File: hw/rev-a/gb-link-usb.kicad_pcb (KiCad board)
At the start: 2 copper layers, 52 x 51 mm, 43 parts, among them J1 10103594-0001LF, J2 TSW-118-07-L-D, J3 TSW-118-07-L-D, J4 SM03B-SRSS-TB(LF)(SN), SW1 434133025816, SW2 434133025816, U1 RP2350A, U2 NCP1117ST33T3G, U3 W25Q128JVSIQ, X1 12MHz

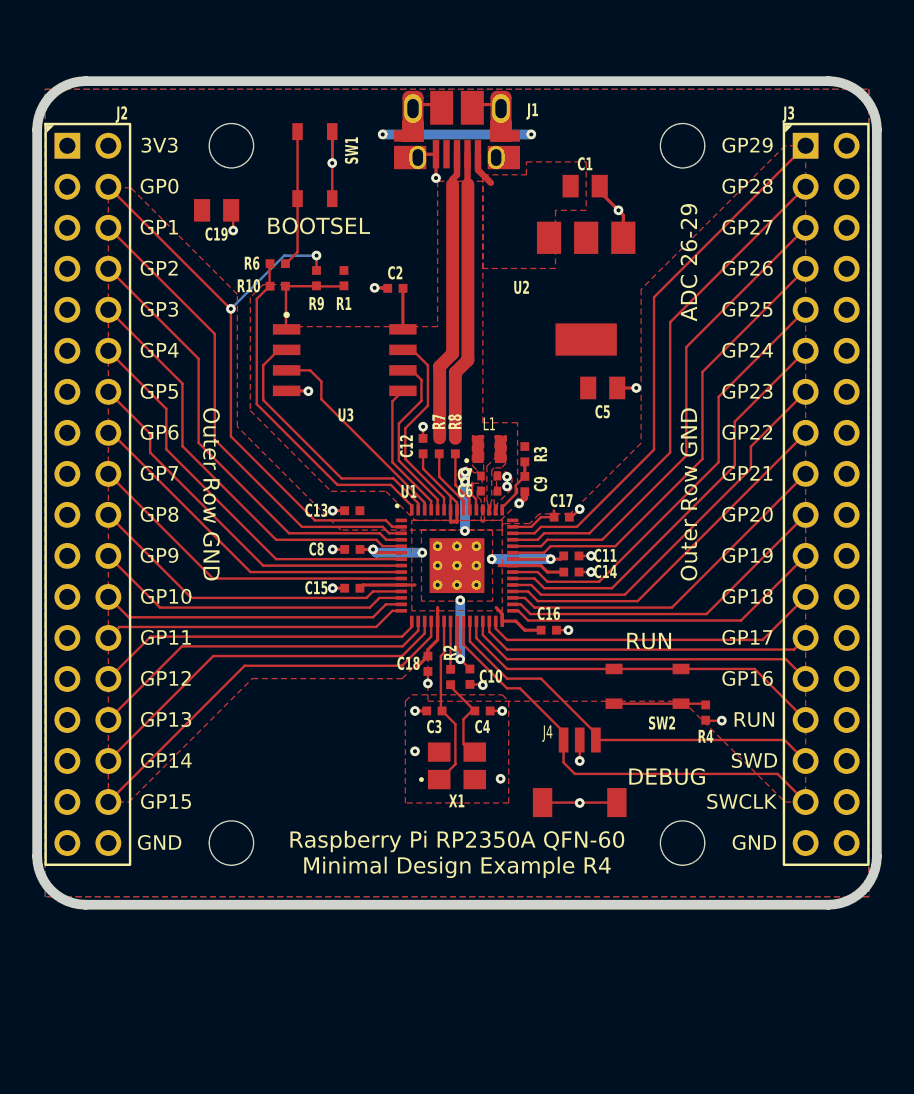
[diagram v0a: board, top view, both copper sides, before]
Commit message: PCB rev A routed: scripted build + Freerouting pipeline, DRC 0 errors
Co-Authored-By: Claude Opus 5.5 (1M context) <noreply@anthropic.com>
Claude-Session: https://claude.ai/code/session_01MZ3uQJCcn6FcjzVDhZnLJN
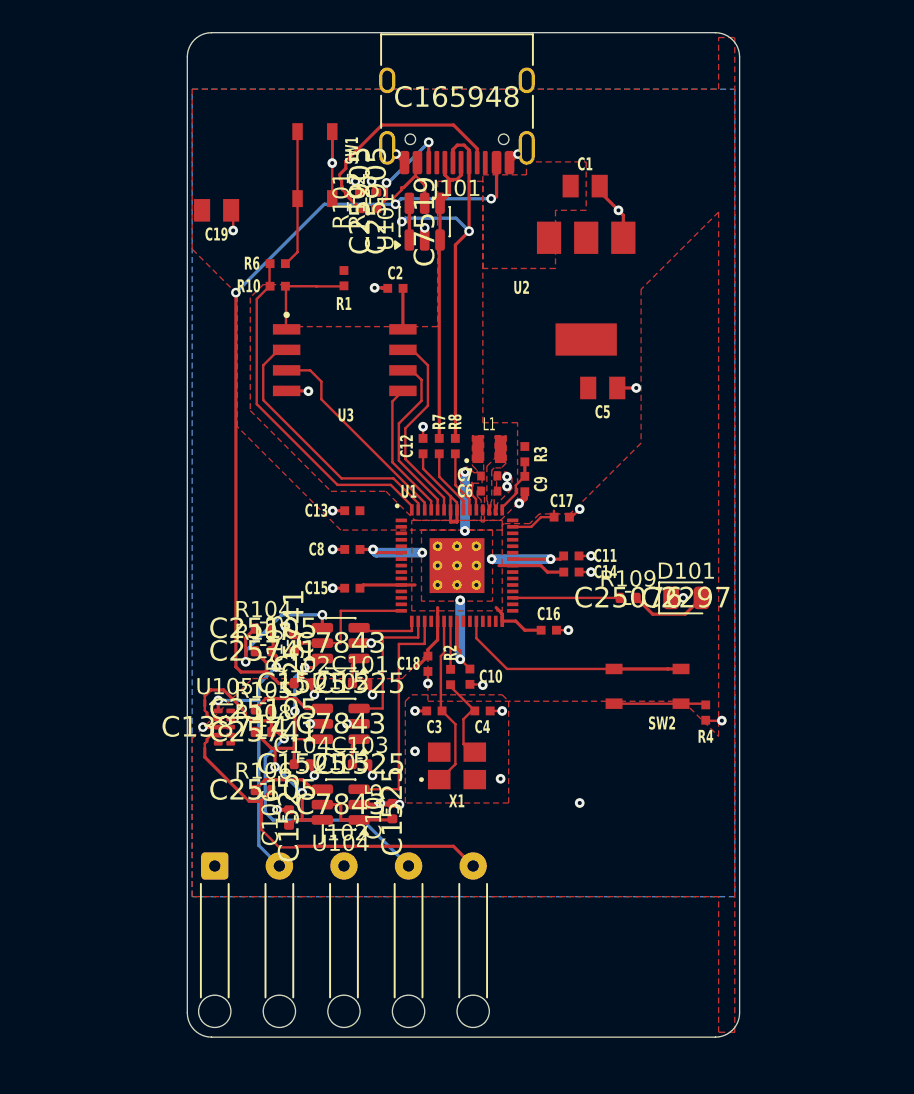
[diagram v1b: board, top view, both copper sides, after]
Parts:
- removed J1: 10103594-0001LF, RPI_COMPILED:amphenol_10103594-0001lf
- removed J2, J3: TSW-118-07-L-D, RPI_COMPILED:samtec_tsw-118-07-l-d
- removed J4: SM03B-SRSS-TB(LF)(SN), RPI_COMPILED:jst_sm03b-srss-tb-lf--sn-
- removed MH1, MH2, MH3, MH4: NPTH FD2.75mm SM3.15mm KO6mm, RPI_COMPILED:none_mh_npth_fd2p75mm_sm3p15mm_ko6mm
- removed R9: 0, RPI_COMPILED:generic_resc1005x35
- added C101: 100n, Capacitor_SMD:C_0402_1005Metric, F.Cu at (94.0, 107.3)
- added C102: 100n, Capacitor_SMD:C_0402_1005Metric, F.Cu at (90.4, 107.3)
- added C103: 100n, Capacitor_SMD:C_0402_1005Metric, F.Cu at (94.0, 112.3)
- added C104: 100n, Capacitor_SMD:C_0402_1005Metric, F.Cu at (90.4, 112.3)
- added C105: 100n, Capacitor_SMD:C_0402_1005Metric, F.Cu at (96.0, 115.2)
- added C106: 100n, Capacitor_SMD:C_0402_1005Metric, F.Cu at (89.6, 115.6)
- added D101: green, LED_SMD:LED_0805_2012Metric, F.Cu at (114.2, 102.0)
- added J101: TYPE-C-31-M-12, Connector_USB:USB_C_Receptacle_HRO_TYPE-C-31-M-12, F.Cu at (100.0, 71.0)
- added J102: Link cable, Connector_Wire:SolderWire-0.15sqmm_1x05_P4mm_D0.5mm_OD1.5mm_Relief, F.Cu at (85.0, 118.6)
- added R101: 5.1k, Resistor_SMD:R_0402_1005Metric, F.Cu at (94.0, 77.4)
- added R102: 5.1k, Resistor_SMD:R_0402_1005Metric, F.Cu at (95.0, 77.4)
- added R103: 100k, Resistor_SMD:R_0402_1005Metric, F.Cu at (89.9, 104.8)
- added R104: 33, Resistor_SMD:R_0402_1005Metric, F.Cu at (88.0, 103.9)
- added R105: 33, Resistor_SMD:R_0402_1005Metric, F.Cu at (88.0, 108.9)
- added R106: 33, Resistor_SMD:R_0402_1005Metric, F.Cu at (88.0, 113.9)
- added R107: 100k, Resistor_SMD:R_0402_1005Metric, F.Cu at (88.0, 105.3)
- added R108: 100k, Resistor_SMD:R_0402_1005Metric, F.Cu at (88.0, 110.3)
- added R109: 100, Resistor_SMD:R_0402_1005Metric, F.Cu at (110.6, 102.0)
- added U101: USBLC6-2SC6, Package_TO_SOT_SMD:SOT-23-6, F.Cu at (98.0, 78.7)
- added U102: SN74LVC1T45DBVR, Package_TO_SOT_SMD:SOT-23-6, F.Cu at (92.8, 104.8)
- added U103: SN74LVC1T45DBVR, Package_TO_SOT_SMD:SOT-23-6, F.Cu at (92.8, 109.8)
- added U104: SN74LVC1T45DBVR, Package_TO_SOT_SMD:SOT-23-6, F.Cu at (92.8, 114.8)
- added U105: TPD4E05U06DQAR, Package_SON:USON-10_2.5x1.0mm_P0.5mm, F.Cu at (85.6, 110.0)
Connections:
- R7 pad 1: /USB_D+ -> USB_D+
- R8 pad 1: /USB_D- -> USB_D-
- U1 pad 10: /GPIO7 -> unconnected-(U1-GPIO7-Pad10)
- U1 pad 12: /GPIO8 -> unconnected-(U1-GPIO8-Pad12)
- U1 pad 13: /GPIO9 -> unconnected-(U1-GPIO9-Pad13)
- U1 pad 14: /GPIO10 -> unconnected-(U1-GPIO10-Pad14)
- U1 pad 15: /GPIO11 -> GPIO11
- U1 pad 16: /GPIO12 -> GPIO12
- U1 pad 17: /GPIO13 -> GPIO13
- U1 pad 18: /GPIO14 -> GPIO14
- U1 pad 19: /GPIO15 -> unconnected-(U1-GPIO15-Pad19)
- U1 pad 2: /GPIO0 -> unconnected-(U1-GPIO0-Pad2)
- U1 pad 24: /SWCLK -> unconnected-(U1-SWCLK-Pad24)
- U1 pad 25: /SWD -> unconnected-(U1-SWDIO-Pad25)
- U1 pad 27: /GPIO16 -> unconnected-(U1-GPIO16-Pad27)
- U1 pad 28: /GPIO17 -> unconnected-(U1-GPIO17-Pad28)
- U1 pad 29: /GPIO18 -> unconnected-(U1-GPIO18-Pad29)
- U1 pad 3: /GPIO1 -> unconnected-(U1-GPIO1-Pad3)
- U1 pad 31: /GPIO19 -> unconnected-(U1-GPIO19-Pad31)
- U1 pad 32: /GPIO20 -> unconnected-(U1-GPIO20-Pad32)
- U1 pad 33: /GPIO21 -> GPIO21
- U1 pad 34: /GPIO22 -> unconnected-(U1-GPIO22-Pad34)
- U1 pad 35: /GPIO23 -> unconnected-(U1-GPIO23-Pad35)
- U1 pad 36: /GPIO24 -> unconnected-(U1-GPIO24-Pad36)
- U1 pad 37: /GPIO25 -> unconnected-(U1-GPIO25-Pad37)
- U1 pad 4: /GPIO2 -> unconnected-(U1-GPIO2-Pad4)
- U1 pad 40: /GPIO26_ADC0 -> unconnected-(U1-GPIO26_ADC0-Pad40)
- U1 pad 41: /GPIO27_ADC1 -> unconnected-(U1-GPIO27_ADC1-Pad41)
- U1 pad 42: /GPIO28_ADC2 -> unconnected-(U1-GPIO28_ADC2-Pad42)
- U1 pad 43: /GPIO29_ADC3 -> unconnected-(U1-GPIO29_ADC3-Pad43)
- U1 pad 5: /GPIO3 -> unconnected-(U1-GPIO3-Pad5)
- U1 pad 7: /GPIO4 -> unconnected-(U1-GPIO4-Pad7)
- U1 pad 8: /GPIO5 -> unconnected-(U1-GPIO5-Pad8)
- U1 pad 9: /GPIO6 -> unconnected-(U1-GPIO6-Pad9)
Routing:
- net VBUS: track 2.11 -> 75.2 mm, vias 0 -> 7
- net /GPIO0: track 39.0 -> 0.00 mm, vias 2 -> 0
- net /GPIO29_ADC3: track 33.6 -> 0.00 mm
- net /GPIO28_ADC2: track 31.9 -> 0.00 mm
- net /GPIO27_ADC1: track 30.3 -> 0.00 mm
- net /GPIO1: track 29.8 -> 0.00 mm
- net /GPIO26_ADC0: track 28.6 -> 0.00 mm
- net /GPIO2: track 28.2 -> 0.00 mm
- net /SWCLK: track 27.8 -> 0.00 mm
- net /GPIO25: track 27.7 -> 0.00 mm
- net USB_D-: track 0.00 -> 27.6 mm, vias 0 -> 2
- net /GPIO3: track 26.5 -> 0.00 mm
- net /GPIO24: track 26.1 -> 0.00 mm
- net /SWD: track 25.4 -> 0.00 mm
- net /GPIO15: track 25.2 -> 0.00 mm
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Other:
- board size 52 x 51 mm -> 34.2 x 62.2 mm
- board text removed: "3V3"
- board text removed: "ADC 26-29"
- board text removed: "BOOTSEL"
- board text removed: "DEBUG"
- board text removed: "GND"
- board text removed: "GP0"
- board text removed: "GP1"
- board text removed: "GP10"
- board text removed: "GP11"
- board text removed: "GP12"
- board text removed: "GP13"
- board text removed: "GP14"
- board text removed: "GP15"
- board text removed: "GP16"
- board text removed: "GP17"
- board text removed: "GP18"
- board text removed: "GP19"
- board text removed: "GP2"
- board text removed: "GP20"
- board text removed: "GP21"
- board text removed: "GP22"
- board text removed: "GP23"
- board text removed: "GP24"
- board text removed: "GP25"
- board text removed: "GP26"
- board text removed: "GP27"
- board text removed: "GP28"
- board text removed: "GP29"
- board text removed: "GP3"
- board text removed: "GP4"
- board text removed: "GP5"
- board text removed: "GP6"
- board text removed: "GP7"
- board text removed: "GP8"
- board text removed: "GP9"
- board text removed: "Minimal Design Example R4"
- board text removed: "Outer Row GND"
- board text removed: "RUN"
- board text removed: "Raspberry Pi RP2350A QFN-60"
- board text removed: "SWCLK"
- board text removed: "SWD"

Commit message: PCB rev A: DRC 0 errors/0 unconnected, silk cleaned, local RPi libs
- TPD4E05U06 NC pins tied for straight-through routing (TI pin table)
- bottom GND pour runs to the board edge (sealed island fix)
- pcb_route retries Freerouting until DRC is clean
- LCSC fields off silk, designators on fab, pad labels
- extract_libs.py: RPi symbols/footprints + lib tables in the project
- renders in hw/rev-a/img

Co-Authored-By: Claude Opus 5.5 (1M context) <noreply@anthropic.com>
Claude-Session: https://claude.ai/code/session_01MZ3uQJCcn6FcjzVDhZnLJN
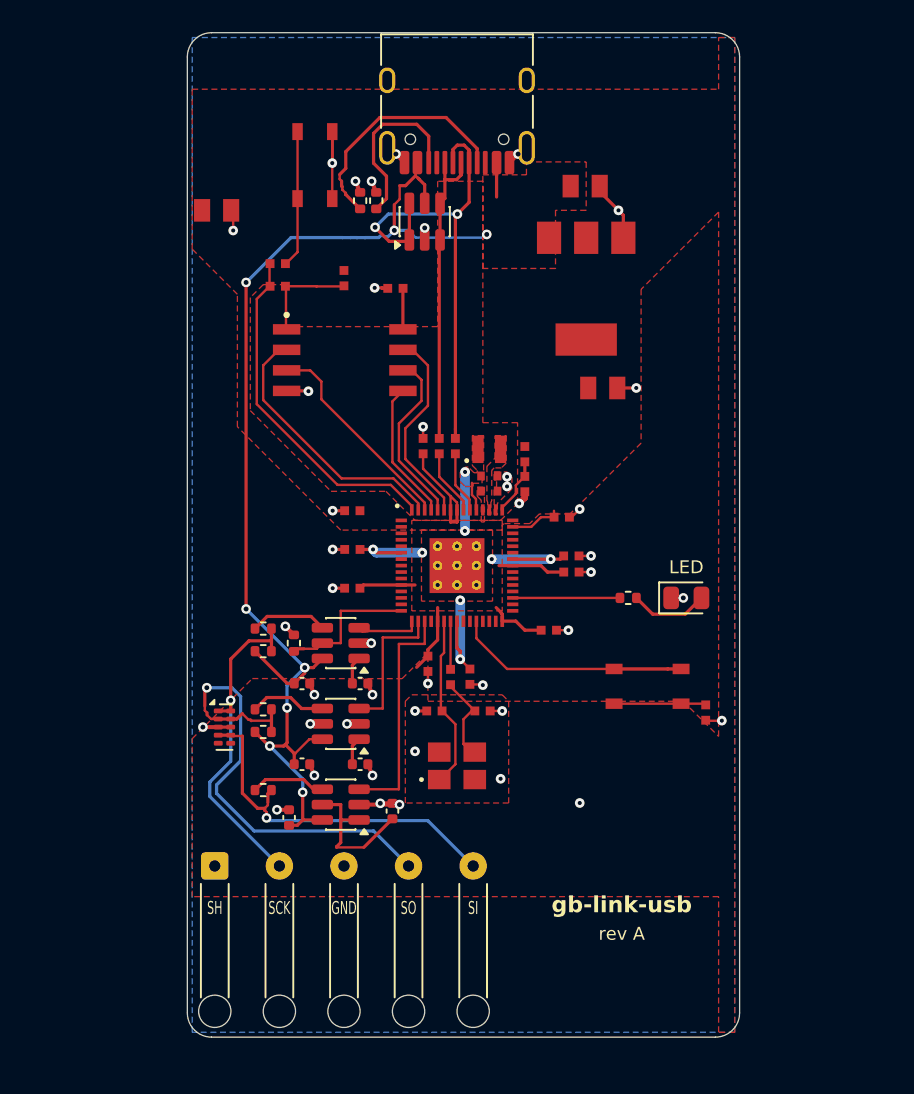
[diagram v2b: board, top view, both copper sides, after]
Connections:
- U105 pad 10: unconnected-(U105-NC-Pad10) -> /Link/LINK_SCK
- U105 pad 7: unconnected-(U105-NC-Pad7) -> /Link/LINK_SI
- U105 pad 9: unconnected-(U105-NC-Pad9) -> /Link/LINK_SO
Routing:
- net /Link/LINK_SO: track 24.9 -> 30.3 mm
- net /Link/B_SCK: track 9.45 -> 4.78 mm, vias 2 -> 0
- net /Link/CC2: track 6.80 -> 10.9 mm, vias 2 -> 0
- net +3V3: track 37.1 -> 41.0 mm
- net USB_D-: track 27.6 -> 30.5 mm
- net /Link/LINK_SCK: track 19.0 -> 20.9 mm, vias 2 -> 1
- net /Link/CC1: track 14.2 -> 14.9 mm
- net /Link/LINK_SI: track 23.4 -> 22.8 mm, vias 0 -> 1
- net VBUS: track 75.2 -> 75.7 mm, vias 7 -> 8
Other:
- board text added: "GND"
- board text added: "LED"
- board text added: "SCK"
- board text added: "SH"
- board text added: "SI"
- board text added: "SO"
- board text added: "gb-link-usb"
- board text added: "rev A"

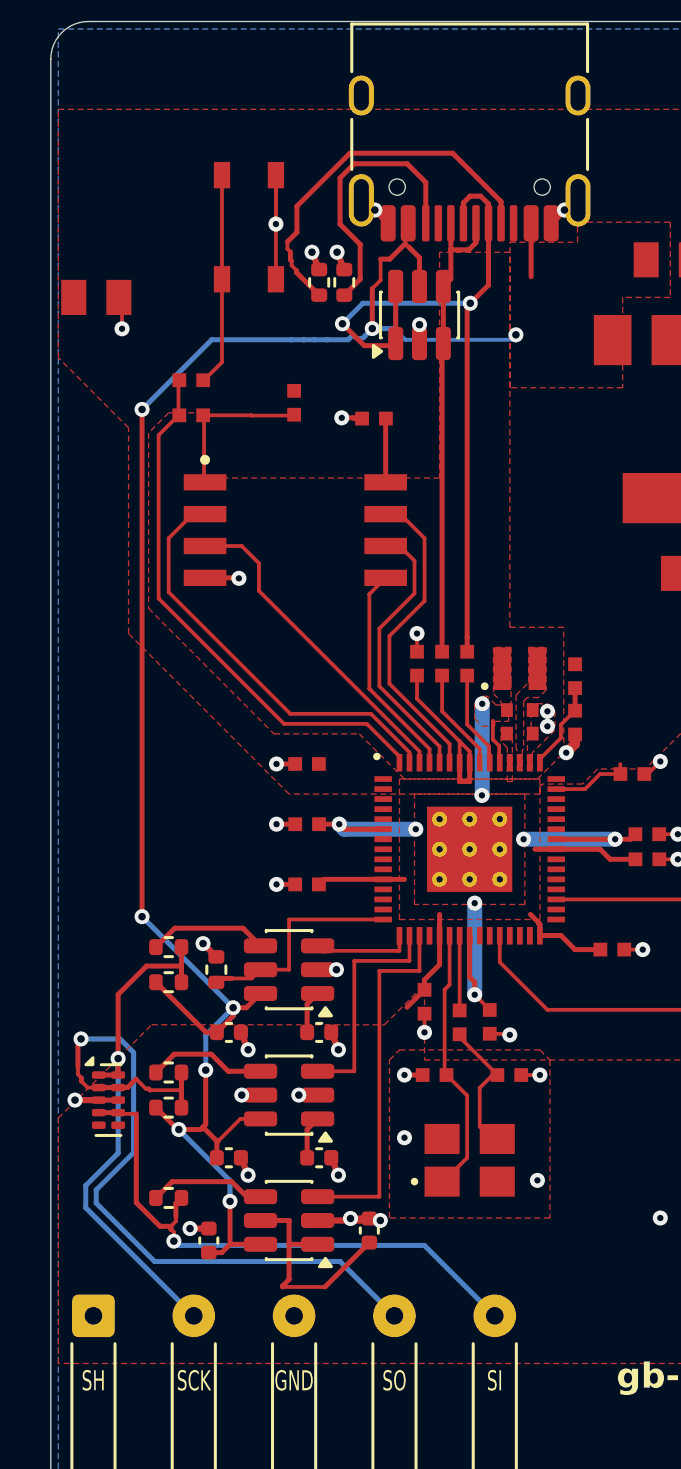
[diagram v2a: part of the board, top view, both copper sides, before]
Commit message: PCB rev A: JLC order files (BOM, CPL, Gerbers, pin audit), core LCSC parts
Not ordered. Hold point: L1 (AOTA-B201610S3R3-101-T) has 4 in JLC stock.
LED pad numbering fixed in the CPL (JLC A=1, KiCad K=1).

Co-Authored-By: Claude Opus 5.5 (1M context) <noreply@anthropic.com>
Claude-Session: https://claude.ai/code/session_01MZ3uQJCcn6FcjzVDhZnLJN
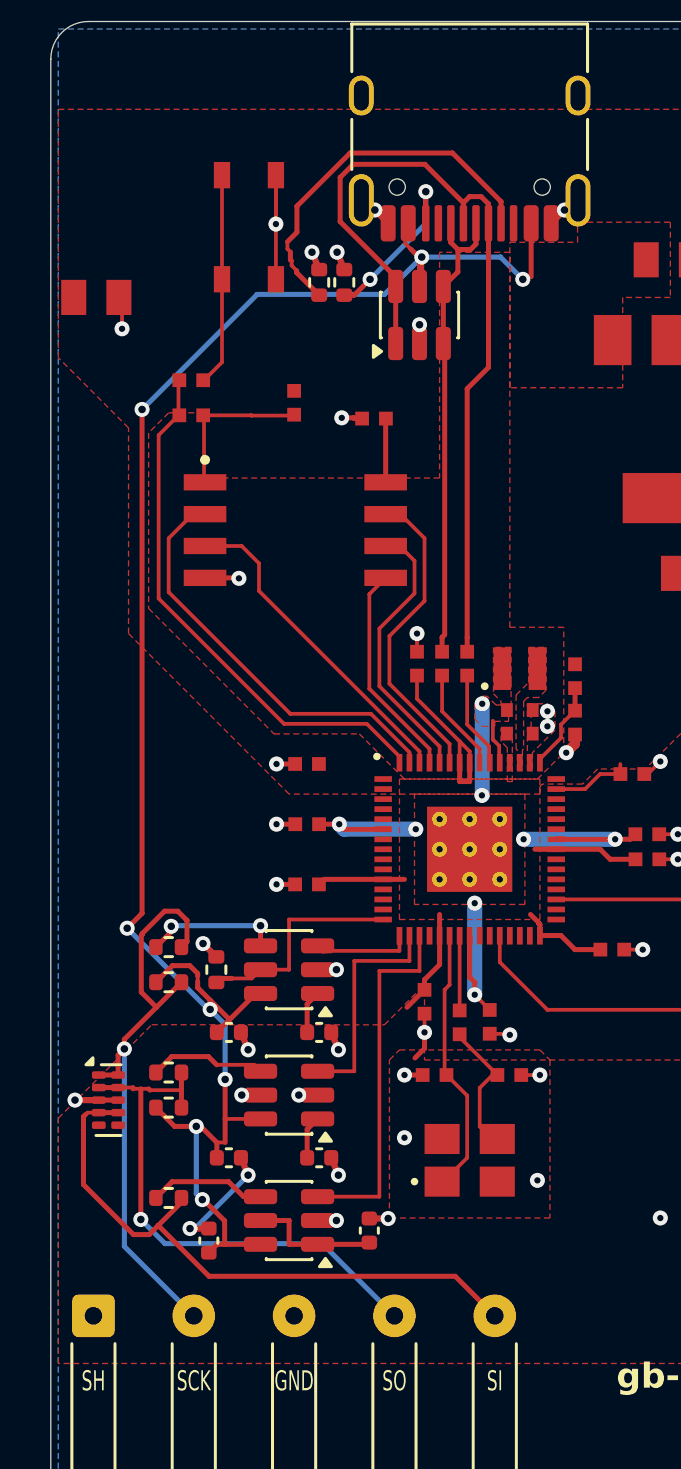
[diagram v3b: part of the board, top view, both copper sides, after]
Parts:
- L1: value 3.3u -> AOTA-B201610S3R3-101-T
- SW1, SW2: value 434133025816 -> SKRPABE010
- X1: value 12MHz -> ABM8-272-T3
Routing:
- net /Link/LINK_SO: track 30.3 -> 21.7 mm
- net +3V3: track 41.0 -> 37.1 mm
- net /Link/CC2: track 10.9 -> 6.97 mm, vias 0 -> 2
- net USB_D-: track 30.5 -> 33.5 mm, vias 2 -> 0
- net /Link/LINK_SCK: track 20.9 -> 24.0 mm
- net GND: track 41.5 -> 44.1 mm
- net /Link/LINK_SI: track 22.8 -> 24.5 mm, vias 1 -> 0
- net /Link/B_SCK: track 4.78 -> 5.46 mm, vias 0 -> 2
